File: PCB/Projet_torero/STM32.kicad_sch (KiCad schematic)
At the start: 32 parts, among them J201 Conn_02x07_Odd_Even, J202 Conn_02x08_Odd_Even, SW201 SW_Push, SW202 SW_Push, U201 STM32G431CBUx, Y201 Crystal_GND24_Small

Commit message: Mis à jour des composants
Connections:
- net +3.3V: no longer C204.1, C205.1, C210.1, C211.1, L202.2, U201.1 (VBAT), U201.20 (VREF+), U201.21 (VDDA)
- new net: C204.1, C205.1, C210.1, C211.1, L202.2, U201.1 (VBAT), U201.20 (VREF+), U201.21 (VDDA)
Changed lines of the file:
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@@
 	(wire
 		(pts
-			(xy 90.17 48.26) (xy 90.17 63.5)
-		)
-		(stroke
-			(width 0)
-			(type default)
-		)
-	)
-	(wire
-		(pts
 			(xy 95.25 36.83) (xy 95.25 53.34)
 		)
@@
 					(unit 1)
 				)
-			)
-		)
-	)
-	(symbol
-		(lib_id "power:+3.3V")
-		(at 90.17 48.26 0)
-		(unit 1)
-		(exclude_from_sim no)
-		(in_bom yes)
-		(on_board yes)
-		(dnp no)
-		(property "Reference" "#PWR0209"
-			(at 90.17 52.07 0)
-			(effects
-				(font
-					(size 1.27 1.27)
-				)
-				(hide yes)
-			)
-		)
-		(property "Value" "+3.3V"
-			(at 86.868 43.942 0)
-			(effects
-				(font
-					(size 1.27 1.27)
-				)
-				(justify left)
-			)
-		)
-		(property "Footprint" ""
-			(at 90.17 48.26 0)
-			(effects
-				(font
-					(size 1.27 1.27)
-				)
-				(hide yes)
-			)
-		)
-		(property "Datasheet" ""
-			(at 90.17 48.26 0)
-			(effects
-				(font
-					(size 1.27 1.27)
-				)
-				(hide yes)
-			)
-		)
-		(property "Description" "Power symbol creates a global label with name \"+3.3V\""
-			(at 90.17 48.26 0)
-			(effects
-				(font
-					(size 1.27 1.27)
-				)
-				(hide yes)
-			)
-		)
-		(pin "1"
-		)
-		(instances
-			(project ""
-				(path "/04e1eb47-a2c4-462b-bef7-377d9515a2c0/6473f9d2-6a99-4702-8d30-7daa8ce98486"
-					(reference "#PWR0209")
-					(unit 1)
-				)
-			)
-			(project "STM32"
-				(path "/ce23f9ec-69da-4971-88ea-98d53a12dc3f"
-					(reference "#PWR?")
-					(unit 1)
-				)

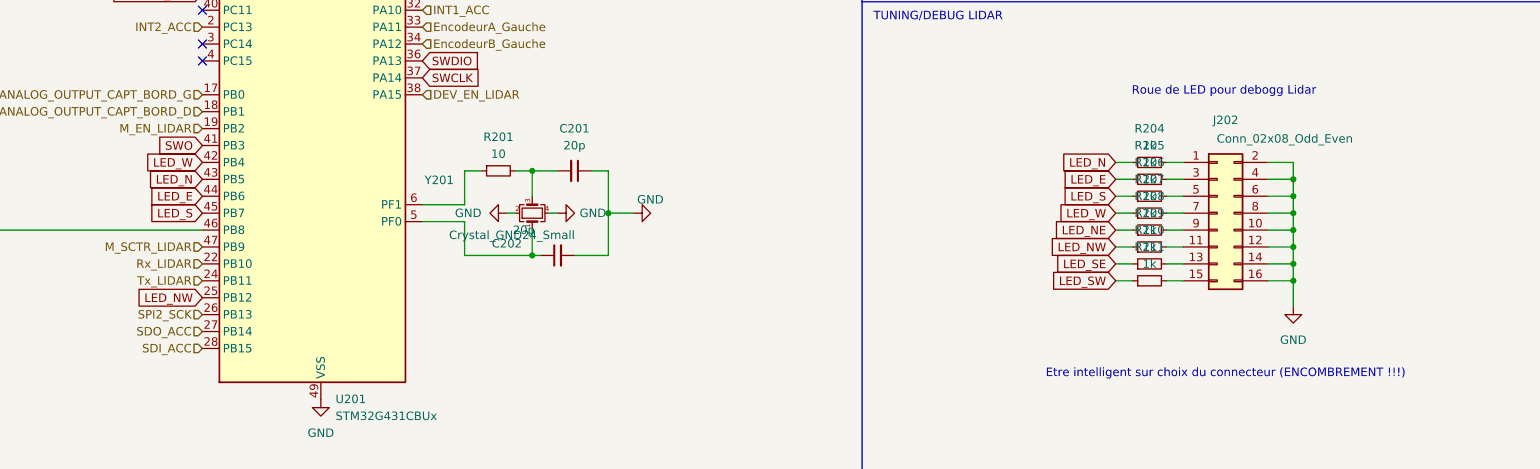
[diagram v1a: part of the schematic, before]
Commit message: Ajout Switch ON/OFF sur carte
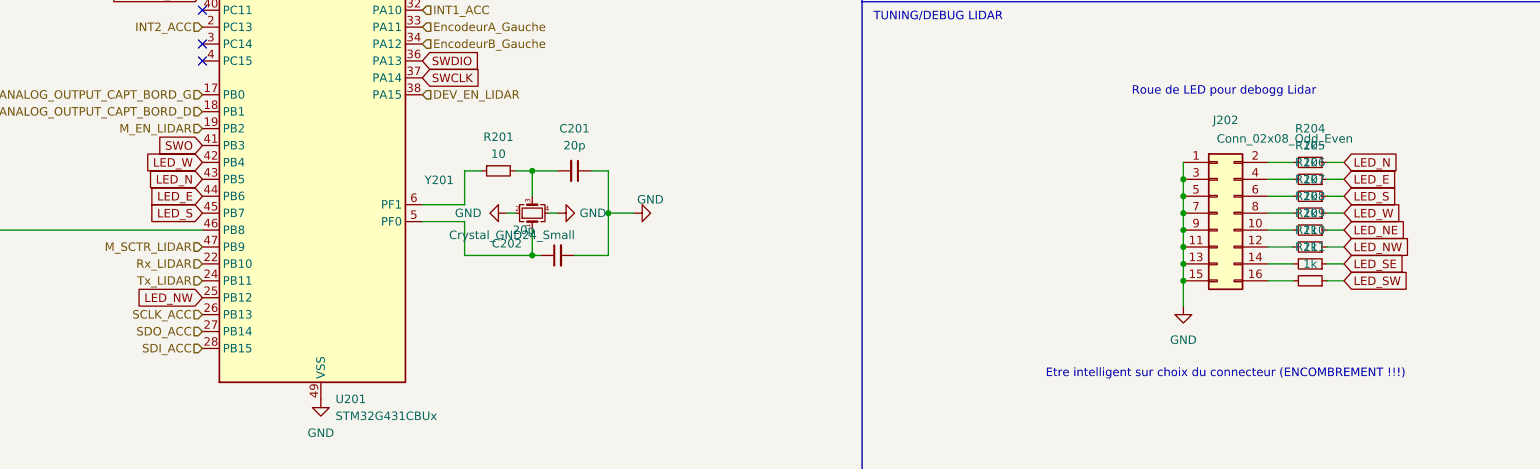
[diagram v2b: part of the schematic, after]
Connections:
- net GND: now also J202.1 (Pin_1), J202.11 (Pin_11), J202.13 (Pin_13), J202.15 (Pin_15), J202.3 (Pin_3), J202.5 (Pin_5), J202.7 (Pin_7), J202.9 (Pin_9); no longer J202.10 (Pin_10), J202.12 (Pin_12), J202.14 (Pin_14), J202.16 (Pin_16), J202.2 (Pin_2), J202.4 (Pin_4), J202.6 (Pin_6), J202.8 (Pin_8)
- net at R211.2: now also J202.16 (Pin_16); no longer J202.15 (Pin_15)
- net at R209.2: now also J202.12 (Pin_12); no longer J202.11 (Pin_11)
- net at R205.2: now also J202.4 (Pin_4); no longer J202.3 (Pin_3)
- net at R204.2: now also J202.2 (Pin_2); no longer J202.1 (Pin_1)
- net at R210.2: now also J202.14 (Pin_14); no longer J202.13 (Pin_13)
- net at R206.2: now also J202.6 (Pin_6); no longer J202.5 (Pin_5)
- net at R207.2: now also J202.8 (Pin_8); no longer J202.7 (Pin_7)
- net at R208.2: now also J202.10 (Pin_10); no longer J202.9 (Pin_9)
- net SPI2_SCK renamed SCLK_ACC
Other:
- moved on the sheet: R204, R205, R206, R207, R208, R209, R210, R211

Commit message: Nouvelle version avec Empreinte correcte
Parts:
- L202: footprint Inductor_SMD:L_0603_1608Metric_Pad1.05x0.95mm_HandSolder -> Inductor_SMD:L_Wuerth_WE-TPC-3816
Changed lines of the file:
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@@
 			)
 		)
-		(property "Footprint" "Inductor_SMD:L_0603_1608Metric_Pad1.05x0.95mm_HandSolder"
+		(property "Footprint" "Inductor_SMD:L_Wuerth_WE-TPC-3816"
 			(at 100.33 58.42 0)
 			(effects

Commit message: Placement des composant "terminé"
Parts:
- added D1: Red, LED_SMD:LED_0603_1608Metric_Pad1.05x0.95mm_HandSolder, symbol Device:LED_Small
- added R314: 140, Resistor_SMD:R_0603_1608Metric, symbol Device:R_Small
- L202: footprint Inductor_SMD:L_Wuerth_WE-TPC-3816 -> Inductor_SMD:L_0603_1608Metric
- R201: footprint Resistor_SMD:R_0603_1608Metric -> Resistor_SMD:R_0402_1005Metric
- Y201: footprint Crystal:Crystal_SMD_EuroQuartz_X22-4Pin_2.5x2.0mm -> Crystal:Crystal_SMD_EuroQuartz_MT-4Pin_3.2x2.5mm
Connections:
- net GND: now also R314.1
- net STATUS_LED_Debug: now reaches U201.40 (PC11)
- net STATUS_LED_Debug: now also D1.2 (A)
- net USER_BTN: now reaches 10k201.2, SW201.1, U201.46 (PB8)
- new net: D1.1 (K), R314.2
- no-connect marks 7 -> 6

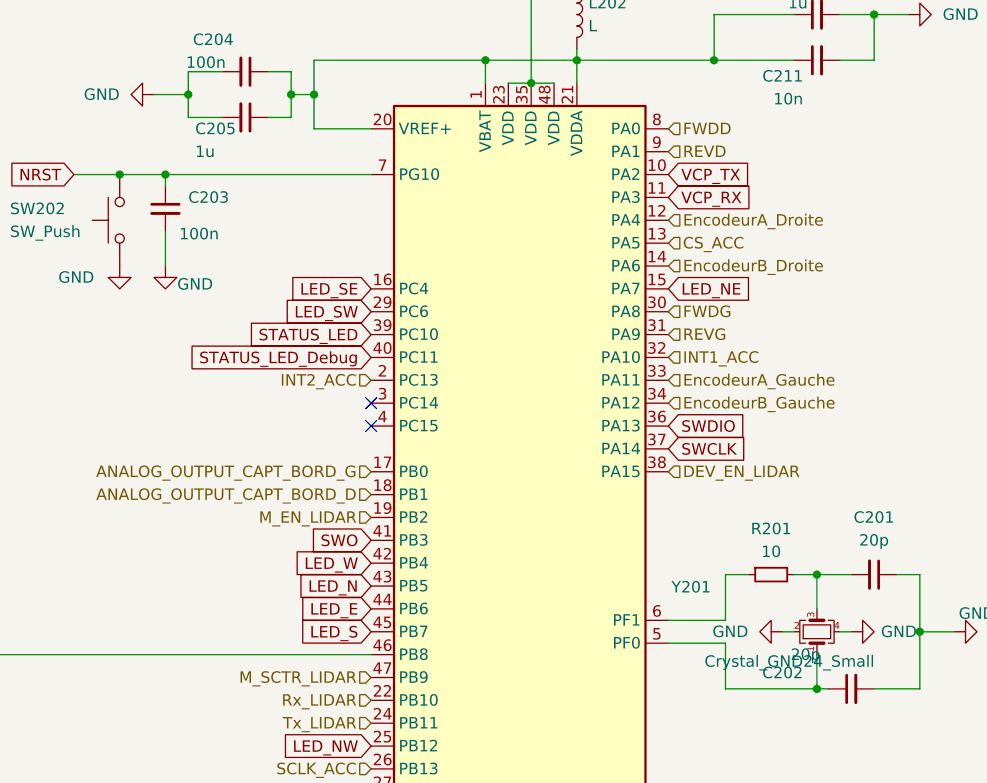
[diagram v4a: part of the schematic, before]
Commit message: changement pin usart2
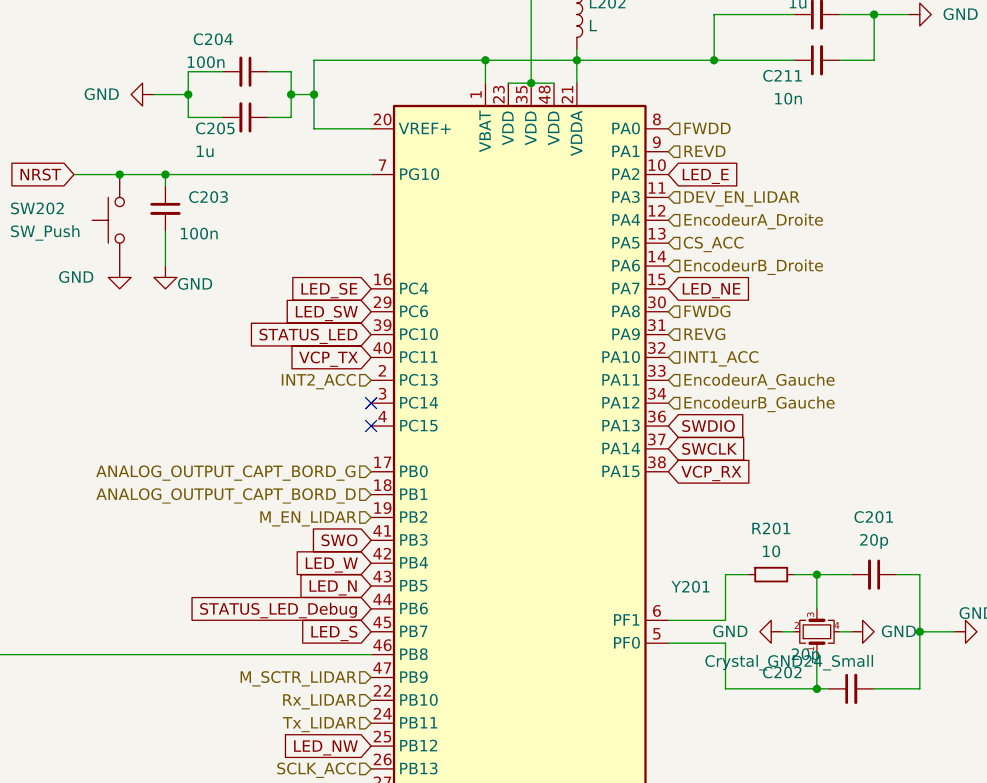
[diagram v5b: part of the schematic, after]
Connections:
- net DEV_EN_LIDAR: now also U201.11 (PA3); no longer U201.38 (PA15)
- net LED_E: now also U201.10 (PA2); no longer U201.44 (PB6)
- net STATUS_LED_Debug: now also U201.44 (PB6); no longer U201.40 (PC11)
- net VCP_RX: now also U201.38 (PA15); no longer U201.11 (PA3)
- net VCP_TX: now also U201.40 (PC11); no longer U201.10 (PA2)

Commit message: rectification erreur pin usart2
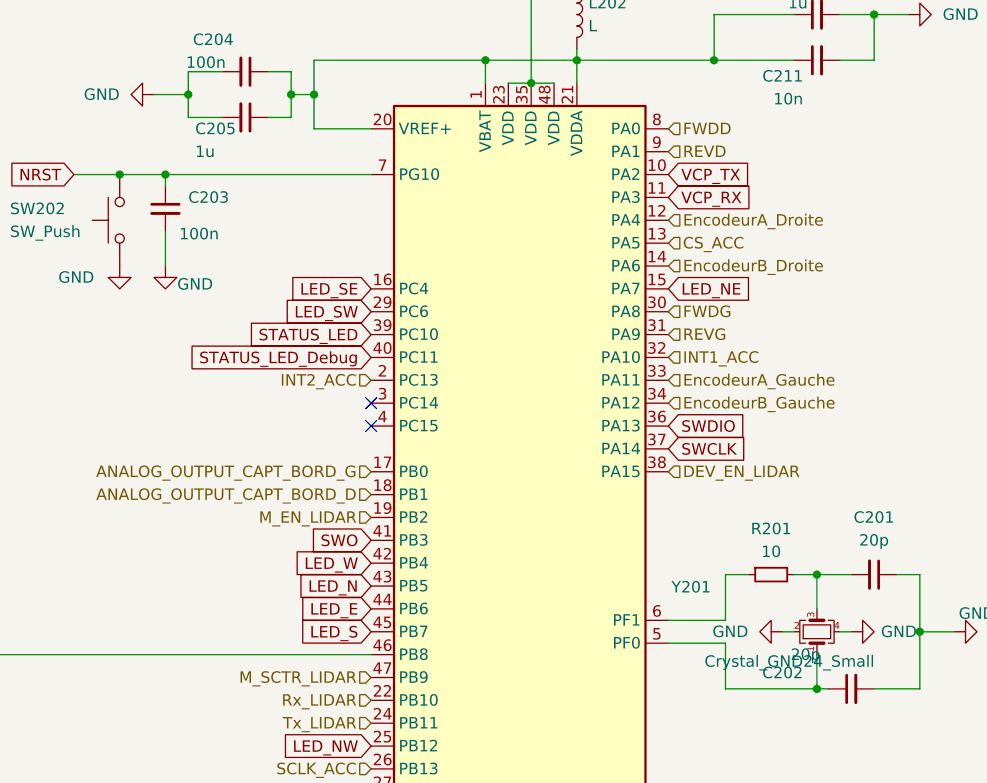
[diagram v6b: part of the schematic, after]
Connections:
- net DEV_EN_LIDAR: now also U201.38 (PA15); no longer U201.11 (PA3)
- net LED_E: now also U201.44 (PB6); no longer U201.10 (PA2)
- net STATUS_LED_Debug: now also U201.40 (PC11); no longer U201.44 (PB6)
- net VCP_RX: now also U201.11 (PA3); no longer U201.38 (PA15)
- net VCP_TX: now also U201.10 (PA2); no longer U201.40 (PC11)
